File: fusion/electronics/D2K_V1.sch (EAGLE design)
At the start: 26 parts, among them M1 Active Cooler SC1148, SW1 BTN_DPAD_UP, SW10 BTN_SELECT, SW11 BTN_HOME, SW12 BTN_L1, SW13 BTN_R1, SW14 BTN_L2, SW15 BTN_R2, SW2 BTN_DPAD_DOWN, SW3 BTN_DPAD_LEFT, SW4 BTN_DPAD_RIGHT, SW5 BTN_A, SW6 BTN_B, SW7 BTN_X, SW8 BTN_Y, SW9 BTN_START, U1 Raspberry Pi 5, U2 ESP32-S3-Zero - USB HID, U3 WM8960 Audio Board

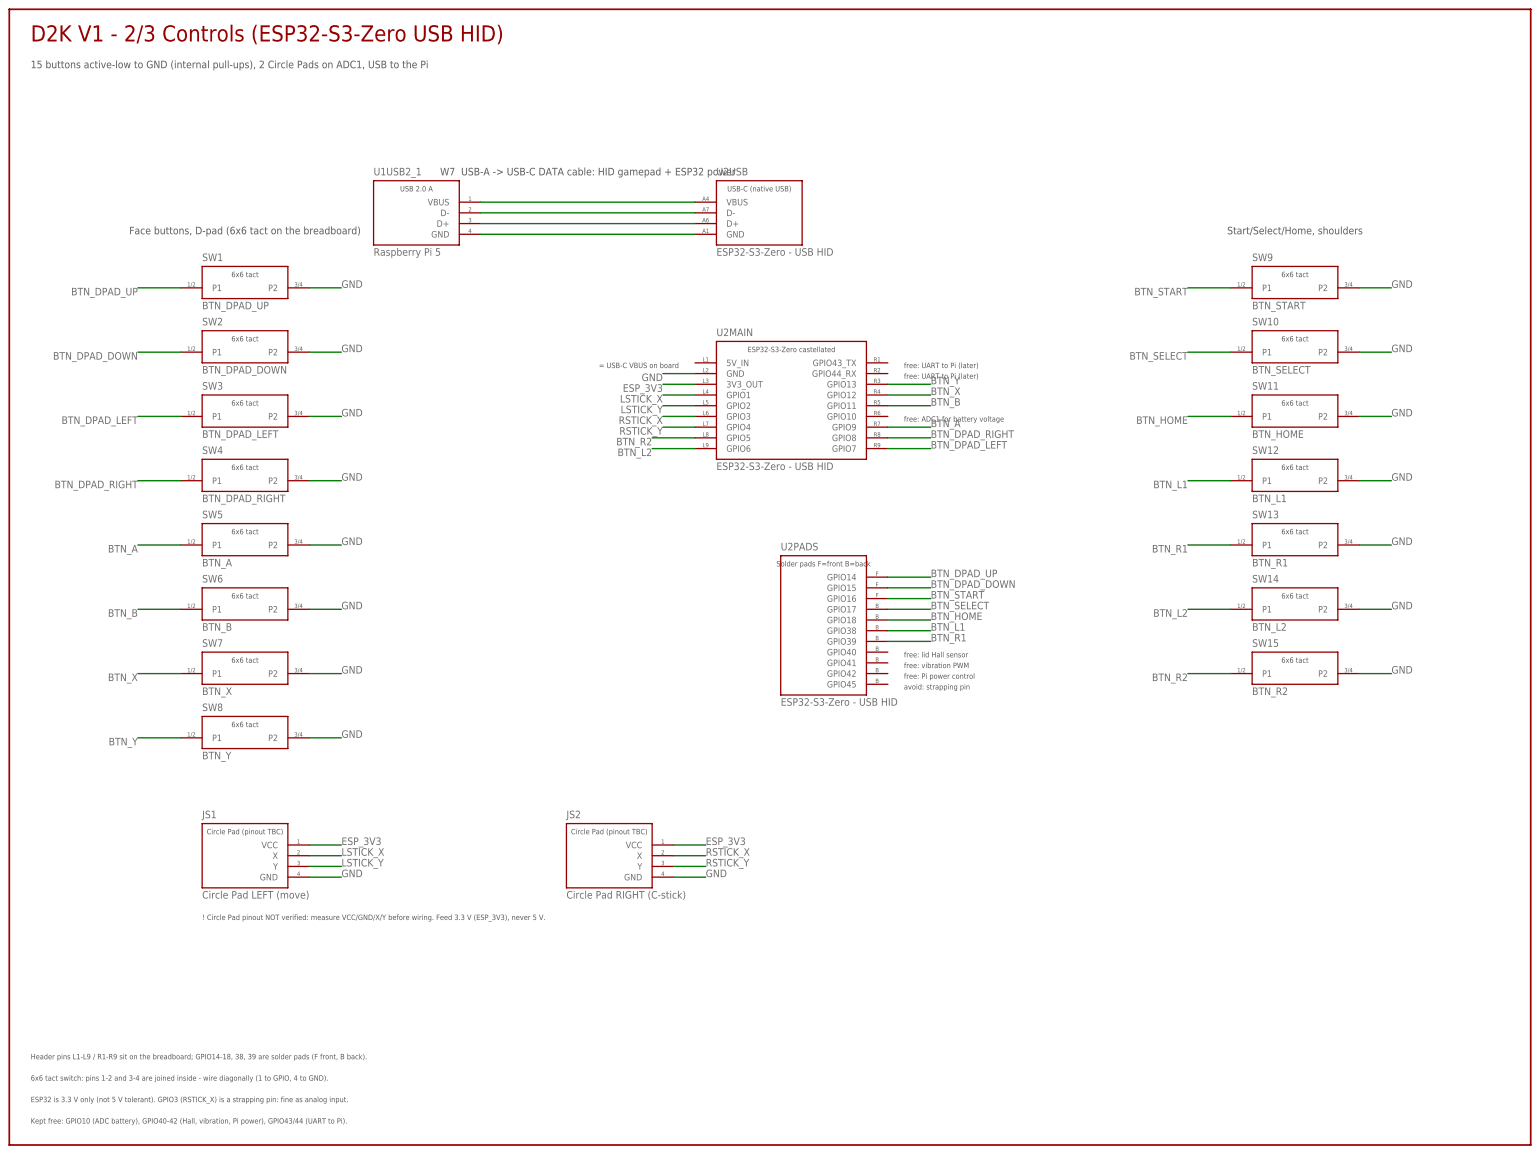
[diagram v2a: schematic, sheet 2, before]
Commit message: Rewire the bench controls without soldering
The Circle Pads are not here yet, so all 15 buttons now use the 15 ESP32
header GPIOs: shoulders on GPIO1-4 until the pads arrive, SELECT on TX.
The breadboard page drops the soldered pad leads and the Circle Pad wires
(shown as "later"), explains how to read hole names, and still checks that
no two wires cross. The schematic hides the Circle Pads behind
STICKS_FITTED; Q22 tracks where the shoulders go once the pads are fitted.

Co-Authored-By: Claude Opus 5.5 <noreply@anthropic.com>
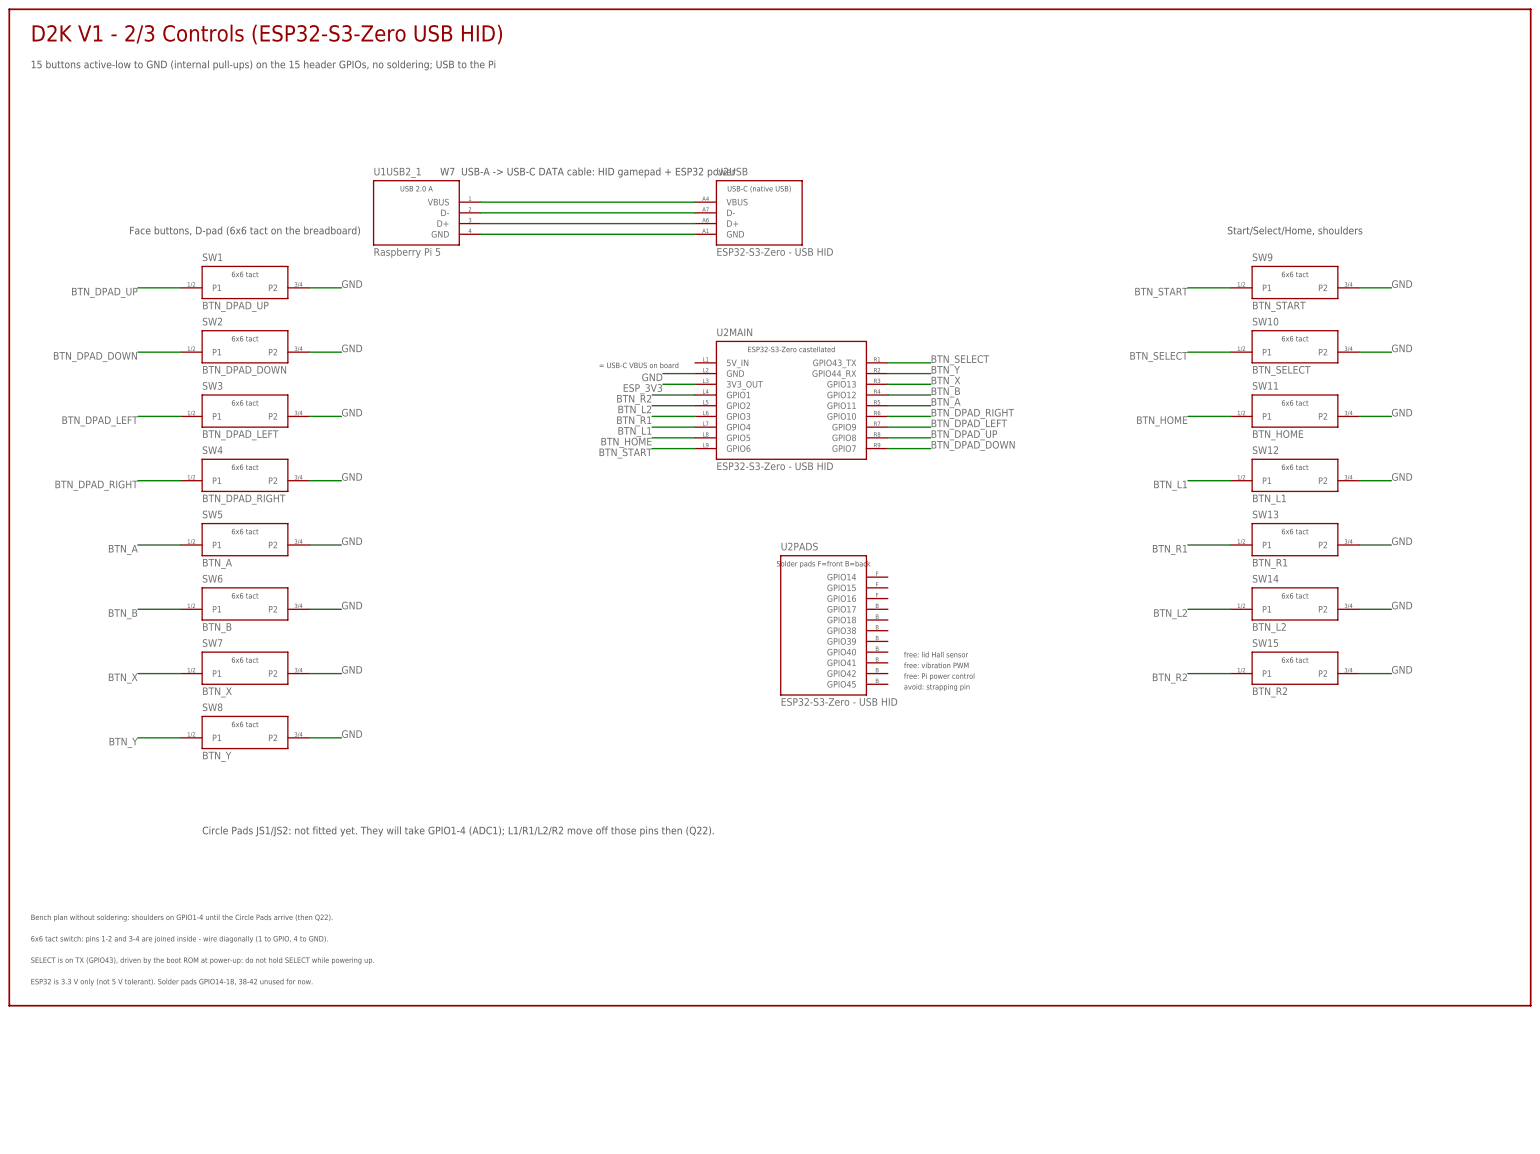
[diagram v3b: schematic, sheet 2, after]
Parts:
- removed JS1: Circle Pad LEFT (move), D2K:CIRCLE_PAD_N3DSXL
- removed JS2: Circle Pad RIGHT (C-stick), D2K:CIRCLE_PAD_N3DSXL
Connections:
- removed net LSTICK_X: JS1.X, U2MAIN.GPIO1
- removed net LSTICK_Y: JS1.Y, U2MAIN.GPIO2
- removed net RSTICK_X: JS2.X, U2MAIN.GPIO3
- removed net RSTICK_Y: JS2.Y, U2MAIN.GPIO4
- net BTN_A: now also U2MAIN.GPIO11; no longer U2MAIN.GPIO9
- net BTN_B: now also U2MAIN.GPIO12; no longer U2MAIN.GPIO11
- net BTN_DPAD_DOWN: now also U2MAIN.GPIO7; no longer U2PADS.GPIO15
- net BTN_DPAD_LEFT: now also U2MAIN.GPIO9; no longer U2MAIN.GPIO7
- net BTN_DPAD_RIGHT: now also U2MAIN.GPIO10; no longer U2MAIN.GPIO8
- net BTN_DPAD_UP: now also U2MAIN.GPIO8; no longer U2PADS.GPIO14
- net BTN_HOME: now also U2MAIN.GPIO5; no longer U2PADS.GPIO18
- net BTN_L1: now also U2MAIN.GPIO4; no longer U2PADS.GPIO38
- net BTN_L2: now also U2MAIN.GPIO2; no longer U2MAIN.GPIO6
- net BTN_R1: now also U2MAIN.GPIO3; no longer U2PADS.GPIO39
- net BTN_R2: now also U2MAIN.GPIO1; no longer U2MAIN.GPIO5
- net BTN_SELECT: now also U2MAIN.GPIO43_TX; no longer U2PADS.GPIO17
- net BTN_START: now also U2MAIN.GPIO6; no longer U2PADS.GPIO16
- net BTN_X: now also U2MAIN.GPIO13; no longer U2MAIN.GPIO12
- net BTN_Y: now also U2MAIN.GPIO44_RX; no longer U2MAIN.GPIO13
- net ESP_3V3: no longer JS1.VCC, JS2.VCC
- net GND: no longer JS1.GND, JS2.GND
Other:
- note added: "15 buttons active-low to GND (internal pull-ups) on the 15 header GPIOs, no soldering; USB to the Pi"
- note added: "Bench plan without soldering: shoulders on GPIO1-4 until the Circle Pads arrive (then Q22)."
- note added: "Circle Pads JS1/JS2: not fitted yet. They will take GPIO1-4 (ADC1); L1/R1/L2/R2 move off those pins then (Q22)."
- note added: "ESP32 is 3.3 V only (not 5 V tolerant). Solder pads GPIO14-18, 38-42 unused for now."
- note added: "SELECT is on TX (GPIO43), driven by the boot ROM at power-up: do not hold SELECT while powering up."
- note removed: "! Circle Pad pinout NOT verified: measure VCC/GND/X/Y before wiring. Feed 3.3 V (ESP_3V3), never 5 V."
- note removed: "15 buttons active-low to GND (internal pull-ups), 2 Circle Pads on ADC1, USB to the Pi"
- note removed: "ESP32 is 3.3 V only (not 5 V tolerant). GPIO3 (RSTICK_X) is a strapping pin: fine as analog input."
- note removed: "Header pins L1-L9 / R1-R9 sit on the breadboard; GPIO14-18, 38, 39 are solder pads (F front, B back)."
- note removed: "Kept free: GPIO10 (ADC battery), GPIO40-42 (Hall, vibration, Pi power), GPIO43/44 (UART to Pi)."
- note removed: "free: ADC1 for battery voltage"
- note removed: "free: UART to Pi (later)"
